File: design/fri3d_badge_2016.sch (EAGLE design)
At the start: 39 parts, among them U1 MCP73831, Y1 8MHz

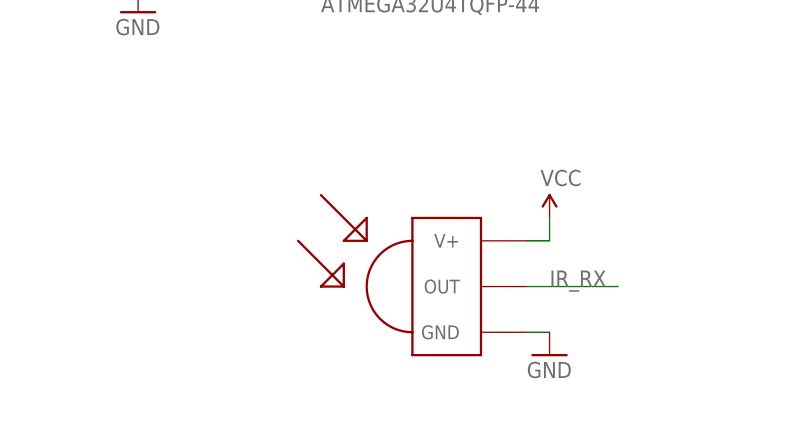
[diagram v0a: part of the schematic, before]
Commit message: added missing cap+resistor on IR Receiver
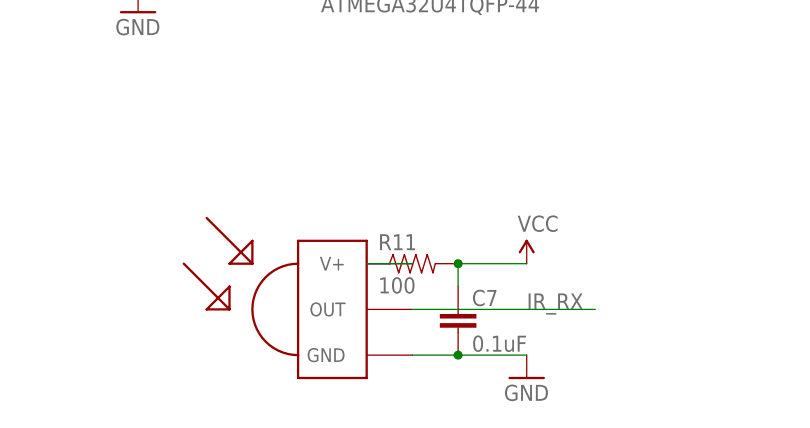
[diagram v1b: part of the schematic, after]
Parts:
- added C7: 0.1uF, SparkFun-Capacitors:CAP0805
- added R11: 100, SparkFun-Passives:RESISTOR0805-RES
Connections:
- new net N$23: R11.1, U$3.V+
- net GND: now also C7.2
- net VCC: now also C7.1, R11.2; no longer U$3.V+
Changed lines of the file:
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@@
 <part name="LED5" library="adafruit" deviceset="LED" device="CHIPLED_0805"/>
 <part name="R10" library="SparkFun-Passives" deviceset="RESISTOR" device="0805-RES" value="64.9"/>
+<part name="R11" library="SparkFun-Passives" deviceset="RESISTOR" device="0805-RES" value="100"/>
+<part name="C7" library="SparkFun-Capacitors" deviceset="CAP" device="0805" value="0.1uF"/>
 </parts>
 <sheets>
@@
 <instance part="GND15" gate="1" x="167.64" y="101.6"/>
 <instance part="GND16" gate="1" x="167.64" y="127"/>
-<instance part="GND17" gate="1" x="101.6" y="22.86"/>
-<instance part="U$3" gate="G$1" x="91.44" y="30.48"/>
-<instance part="SUPPLY7" gate="G$1" x="101.6" y="38.1"/>
+<instance part="GND17" gate="1" x="99.06" y="20.32"/>
+<instance part="U$3" gate="G$1" x="78.74" y="27.94"/>
+<instance part="SUPPLY7" gate="G$1" x="99.06" y="33.02"/>
 <instance part="SUPPLY8" gate="G$1" x="12.7" y="35.56"/>
 <instance part="GND18" gate="1" x="12.7" y="22.86"/>
 <instance part="LED5" gate="G$1" x="-22.86" y="96.52"/>
 <instance part="R10" gate="G$1" x="-15.24" y="88.9"/>
+<instance part="R11" gate="G$1" x="86.36" y="33.02"/>
+<instance part="C7" gate="G$1" x="91.44" y="25.4"/>
 </instances>
 <busses>
@@
 <pinref part="U$3" gate="G$1" pin="GND"/>
 <pinref part="GND17" gate="1" pin="GND"/>
-<wire x1="101.6" y1="25.4" x2="99.06" y2="25.4" width="0.1524" layer="91"/>
+<wire x1="99.06" y1="22.86" x2="91.44" y2="22.86" width="0.1524" layer="91"/>
+<pinref part="C7" gate="G$1" pin="2"/>
+<wire x1="91.44" y1="22.86" x2="86.36" y2="22.86" width="0.1524" layer="91"/>
+<junction x="91.44" y="22.86"/>
 </segment>
 <segment>
@@
 </segment>
 <segment>
-<pinref part="U$3" gate="G$1" pin="V+"/>
 <pinref part="SUPPLY7" gate="G$1" pin="VCC"/>
-<wire x1="101.6" y1="38.1" x2="101.6" y2="35.56" width="0.1524" layer="91"/>
-<wire x1="101.6" y1="35.56" x2="99.06" y2="35.56" width="0.1524" layer="91"/>
+<wire x1="99.06" y1="33.02" x2="91.44" y2="33.02" width="0.1524" layer="91"/>
+<pinref part="R11" gate="G$1" pin="2"/>
+<pinref part="C7" gate="G$1" pin="1"/>
+<wire x1="91.44" y1="30.48" x2="91.44" y2="33.02" width="0.1524" layer="91"/>
+<junction x="91.44" y="33.02"/>
 </segment>
 <segment>
@@
 <segment>
 <pinref part="U$3" gate="G$1" pin="OUT"/>
-<wire x1="99.06" y1="30.48" x2="109.22" y2="30.48" width="0.1524" layer="91"/>
-<label x="101.6" y="30.48" size="1.778" layer="95"/>
+<wire x1="86.36" y1="27.94" x2="106.68" y2="27.94" width="0.1524" layer="91"/>
+<label x="99.06" y="27.94" size="1.778" layer="95"/>
 </segment>
 <segment>
@@
 </segment>
 </net>
+<net name="N$23" class="0">
+<segment>
+<pinref part="U$3" gate="G$1" pin="V+"/>
+<pinref part="R11" gate="G$1" pin="1"/>
+<wire x1="81.28" y1="33.02" x2="86.36" y2="33.02" width="0.1524" layer="91"/>
+</segment>
+</net>

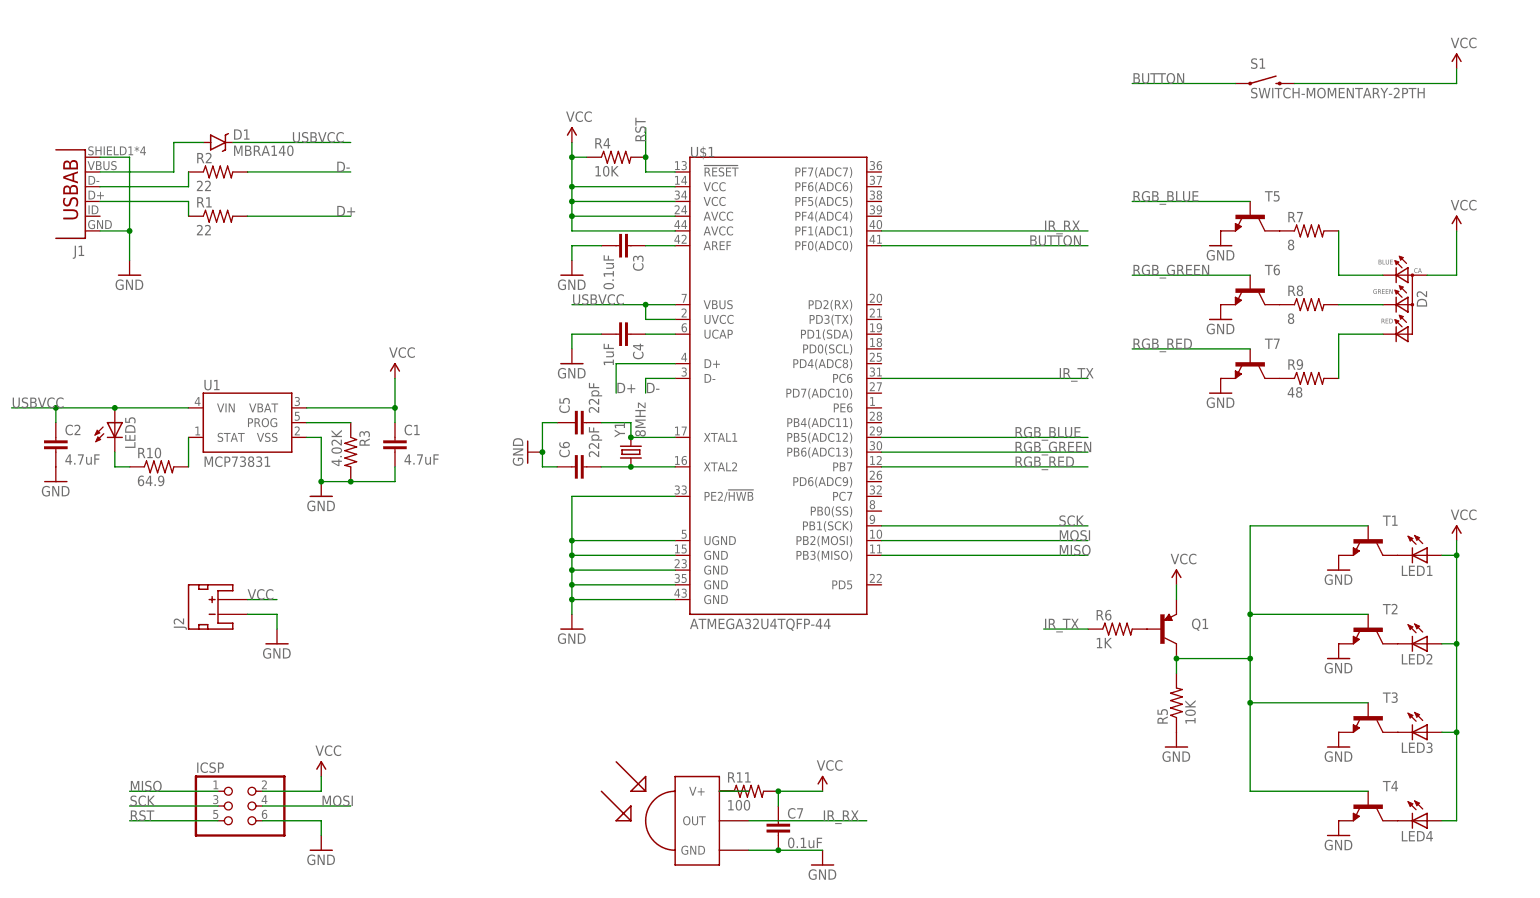
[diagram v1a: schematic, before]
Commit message: update of design based on feedback by Dragan
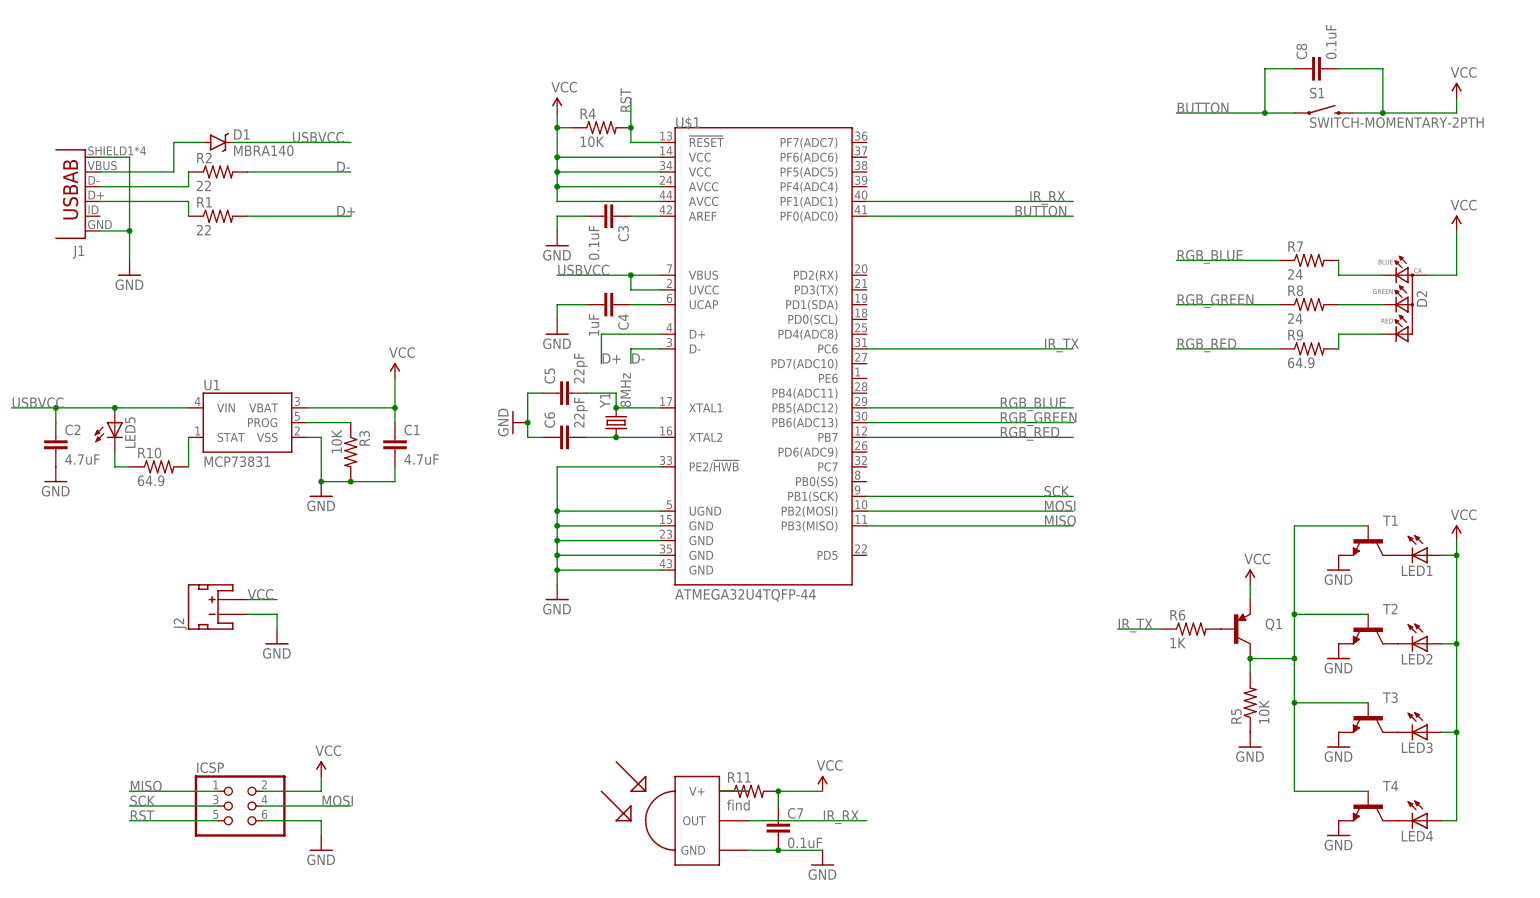
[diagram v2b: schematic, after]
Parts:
- removed T5, T6, T7: (no value), transistor-neu-to92:-NPN-SOT223
- added C8: 0.1uF, SparkFun-Capacitors:CAP0805
- R11: value 100 -> find
- R3: value 4.02K -> 10K
- R7, R8: value 8 -> 24
- R9: value 48 -> 64.9
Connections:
- removed net N$16: R7.1, T5.C
- removed net N$17: R8.1, T6.C
- removed net N$18: R9.1, T7.C
- net BUTTON: now also C8.1
- net GND: no longer T5.E, T6.E, T7.E
- net RGB_BLUE: now also R7.1; no longer T5.B
- net RGB_GREEN: now also R8.1; no longer T6.B
- net RGB_RED: now also R9.1; no longer T7.B
- net VCC: now also C8.2
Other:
- moved on the sheet: C3, C4, C5, C6, Q1, R4, R5, R6, R7, R9, S1, U$1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

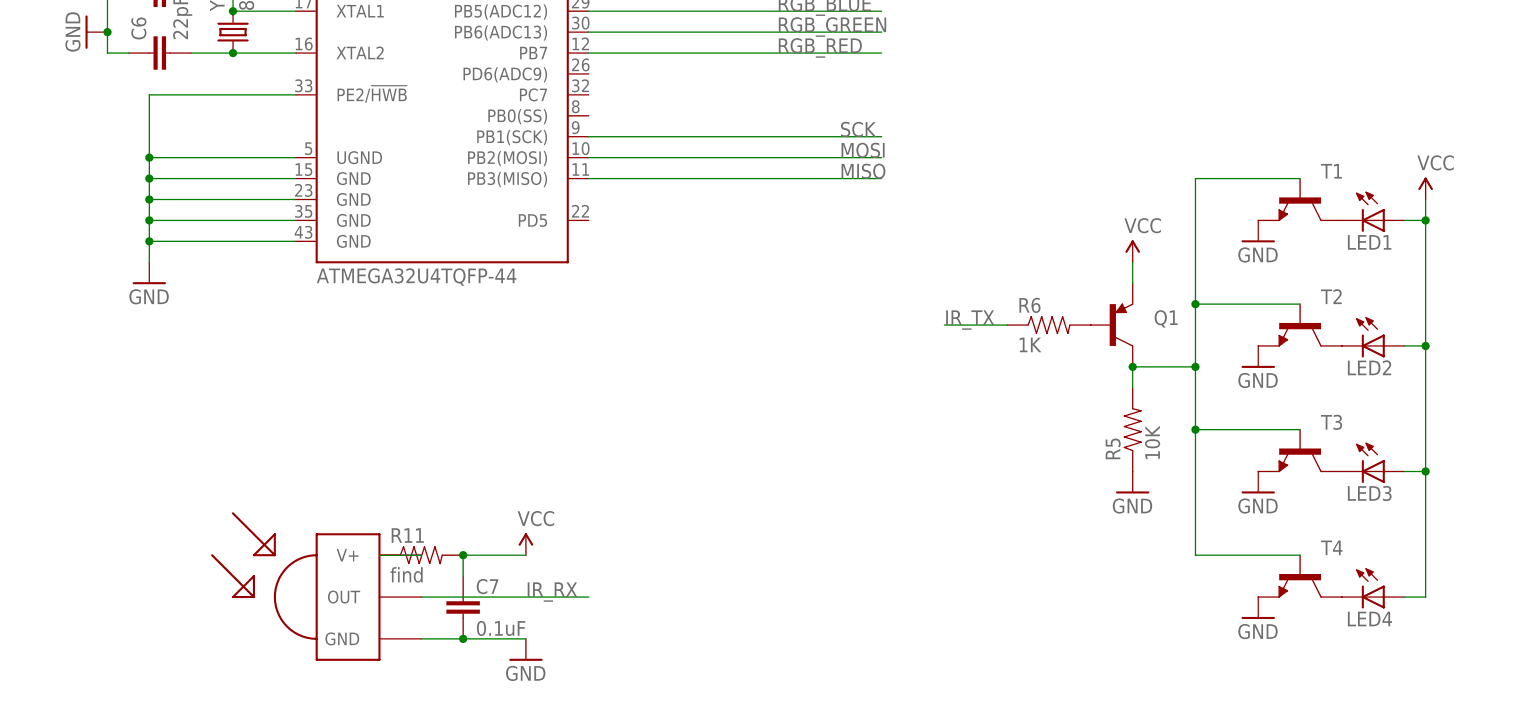
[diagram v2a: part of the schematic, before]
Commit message: added resistors for IR LEDs
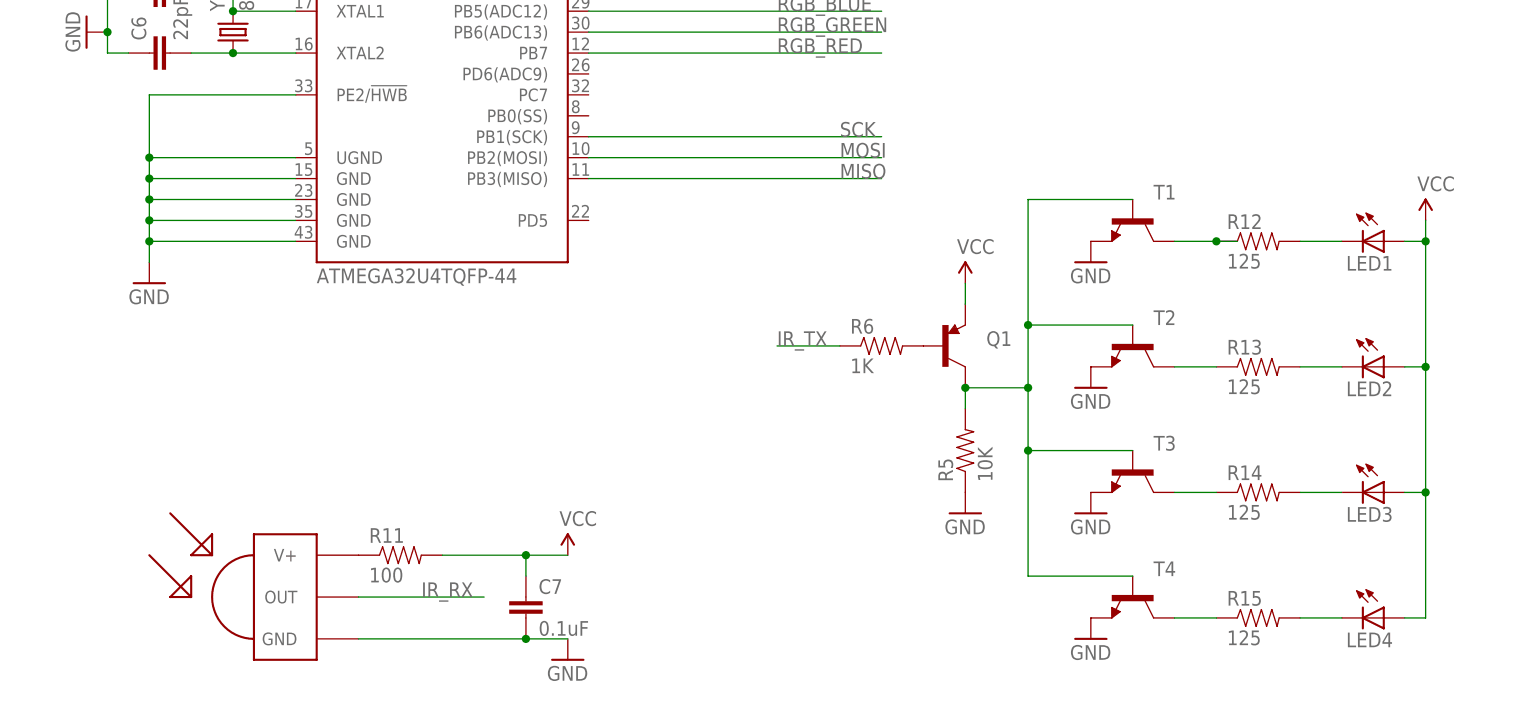
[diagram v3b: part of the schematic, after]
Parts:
- added R12, R13, R14, R15: 125, SparkFun-Passives:RESISTOR0805-RES
- R11: value find -> 100
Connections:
- new net N$17: LED3.C, R14.2
- new net N$18: R14.1, T3.C
- new net N$23: LED4.C, R15.2
- new net N$24: R15.1, T4.C
- net N$12: now also R12.1, T1.C; no longer LED4.C, T4.C
- net N$13: now also LED1.C, R12.2; no longer LED3.C, T3.C
- net N$14: now also R13.2; no longer T2.C
- net N$15: now also R13.1, T2.C; no longer LED1.C, T1.C
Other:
- moved on the sheet: C7, LED1, LED2, LED3, LED4, Q1, R11, R5, R6, T1, T2, T3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
